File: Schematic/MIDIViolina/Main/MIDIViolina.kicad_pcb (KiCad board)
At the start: 2 copper layers, 148.6 x 100.3 mm, 156 parts, among them J1 Motor, J10 STEPPER OUT, J11 Solenoid, J12 Solenoid, J13 Solenoid, J14 Solenoid, J15 Solenoid, J16 Solenoid, J17 Solenoid, J18 Solenoid, J19 Solenoid, J2 Motor, J20 Solenoid, J21 Solenoid, J22 Solenoid, J23 Solenoid, J24 Solenoid, J25 Solenoid, J26 Solenoid, J27 Solenoid, J28 Solenoid, J29 Solenoid, J3 Motor, J30 Solenoid, J31 Solenoid, J32 Solenoid, J33 Solenoid, J34 Solenoid, J35 Solenoid, J36 Solenoid, J37 Solenoid, J38 Solenoid, J39 Solenoid, J4 Motor, J40 Solenoid, J41 Solenoid, J42 Solenoid, J5 Power in, J6 MSB 2, J7 Solenoid, J8 Microstep Bridge, J9 MIDI I/O, Q1 IRF540N, Q10 IRF540N, Q11 IRF540N, Q12 IRF540N, Q13 IRF540N, Q14 IRF540N, Q15 IRF540N, Q16 IRF540N, Q17 IRF540N, Q18 IRF540N, Q19 IRF540N, Q2 IRF540N, Q20 IRF540N, Q21 IRF540N, Q22 IRF540N, Q23 IRF540N, Q24 IRF540N, Q25 IRF540N, Q26 IRF540N, Q27 IRF540N, Q28 IRF540N, Q29 IRF540N, Q3 IRF540N, Q30 IRF540N, Q31 IRF540N, Q32 IRF540N, Q33 IRF540N, Q34 IRF540N, Q35 IRF540N, Q36 IRF540N, Q37 IRF540N, Q4 IRF540N, Q5 IRF540N, Q6 IRF540N, Q7 IRF540N, Q8 IRF540N, Q9 IRF540N, U1 LM7805_TO220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

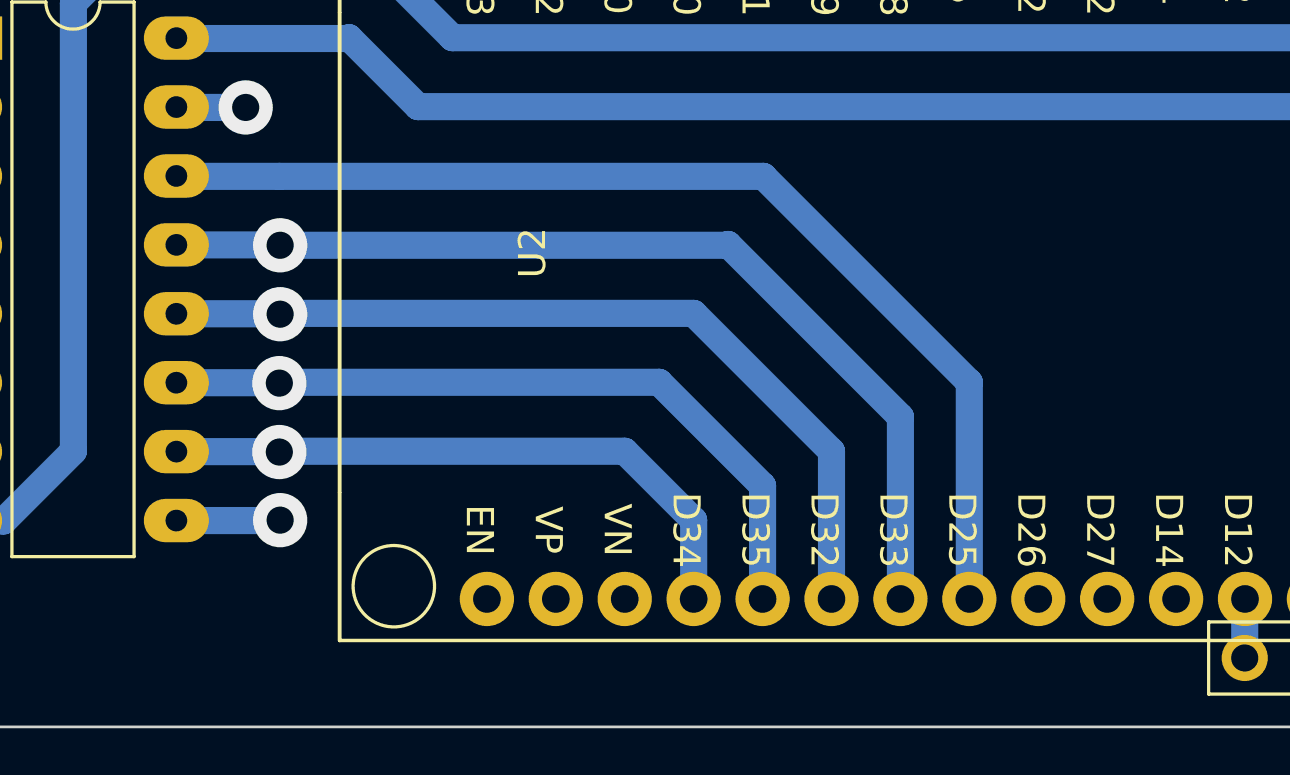
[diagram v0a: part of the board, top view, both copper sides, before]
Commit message: some schematic updates
found a pinout error where I had them hooked up to "input only" pins. Corrected this issue.
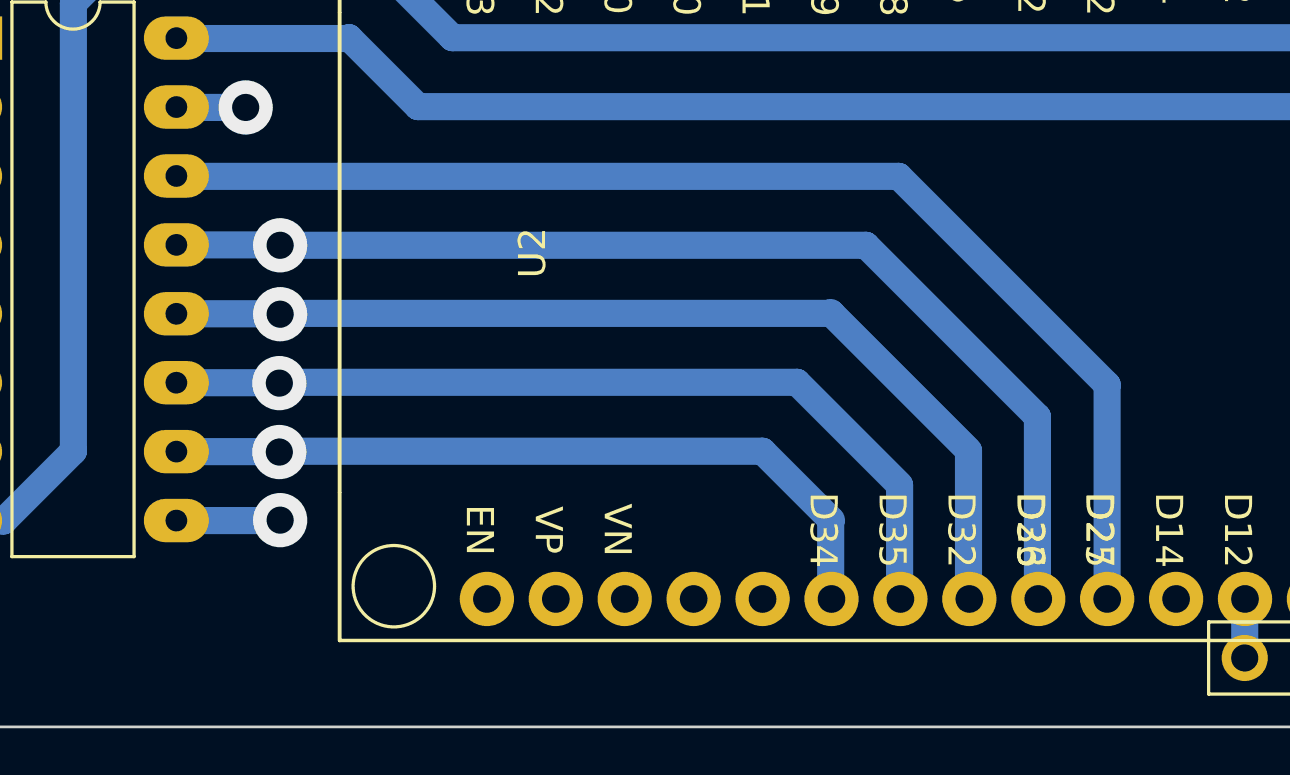
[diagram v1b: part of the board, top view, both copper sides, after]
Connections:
- U2 pad 19: SHIFT CLEAR -> unconnected-(U2-Pad19)
- U2 pad 20: SHIFT CLOCK -> unconnected-(U2-Pad20)
- U2 pad 21: LATCH -> SHIFT CLEAR
- U2 pad 22: OUT ENABLE -> SHIFT CLOCK
- U2 pad 23: SHIFT I/O -> LATCH
- U2 pad 24: unconnected-(U2-Pad24) -> OUT ENABLE
- U2 pad 25: unconnected-(U2-Pad25) -> SHIFT I/O
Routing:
- net SHIFT I/O: track 40.0 -> 45.4 mm
- net LATCH: track 39.0 -> 44.0 mm
- net SHIFT CLEAR: track 30.3 -> 35.4 mm
- net SHIFT CLOCK: track 34.6 -> 39.7 mm
- net OUT ENABLE: track 99.2 -> 104.2 mm
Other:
- board text added: "N:U Input Only"

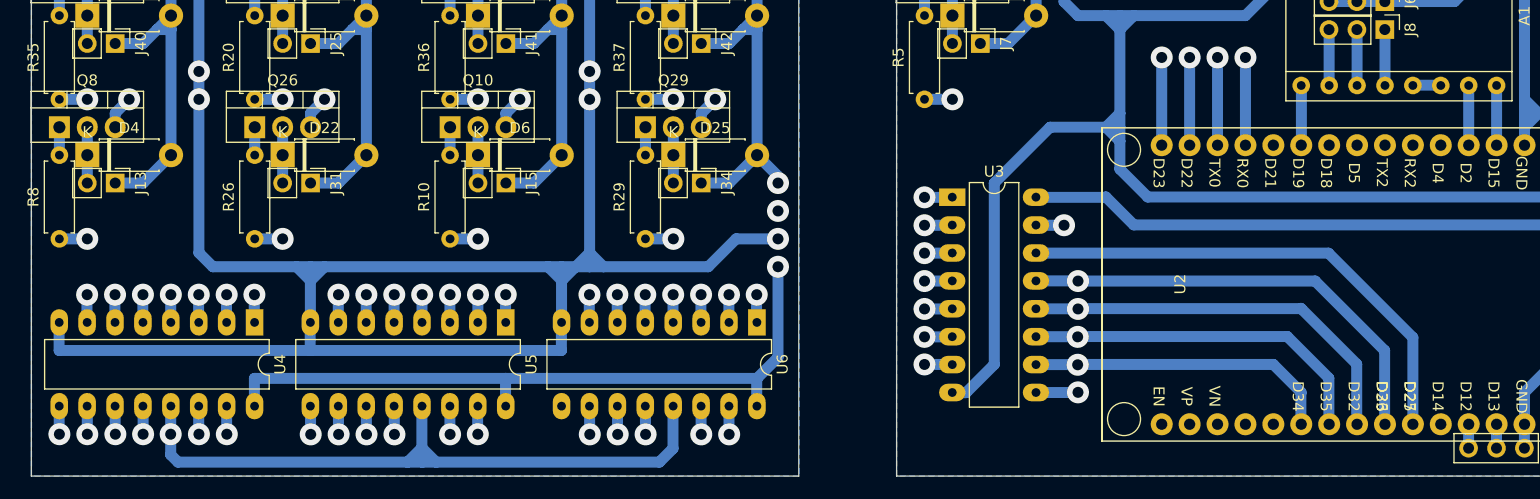
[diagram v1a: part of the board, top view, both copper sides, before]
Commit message: fix pin routing problems
added extra thru-vias and corrected pinouts
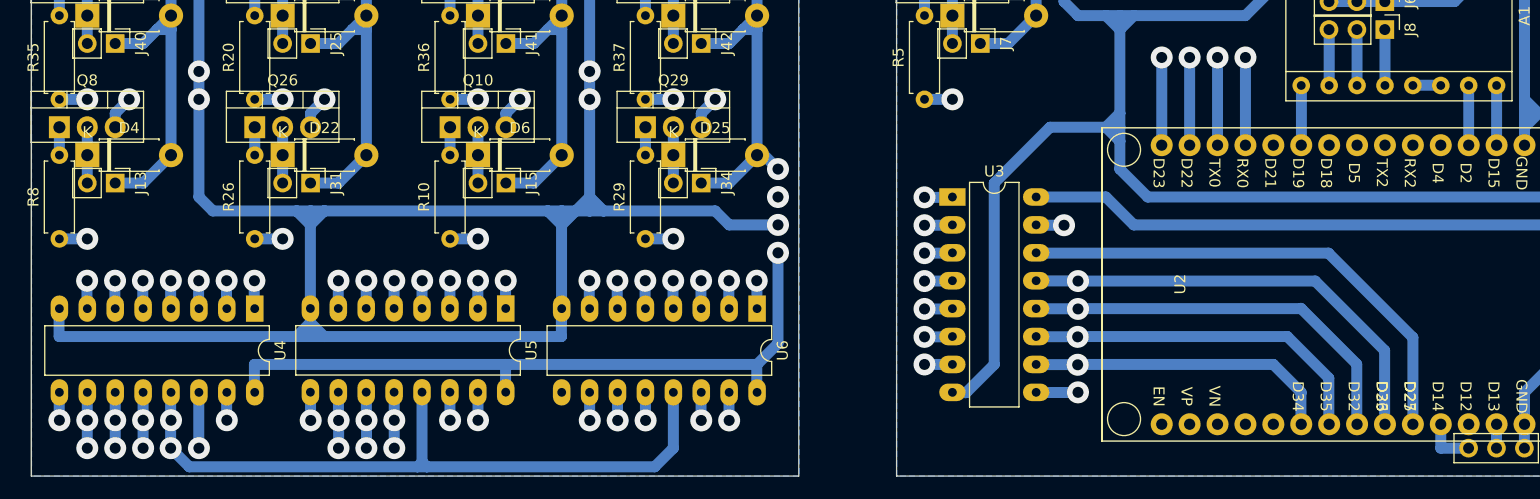
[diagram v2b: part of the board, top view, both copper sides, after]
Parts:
- moved U5 1.27 mm to (113.0, 124.4)
- moved U4 1.26 mm to (90.2, 124.5)
- moved U6 1.26 mm to (135.9, 124.5)
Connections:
- U2 pad 26: unconnected-(U2-Pad26) -> Net-(J9-Pad4)
- U2 pad 27: Net-(J9-Pad4) -> unconnected-(U2-Pad27)
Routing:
- net SHIFT CLOCK: track 39.7 -> 44.8 mm, vias 4 -> 6
- net LATCH: track 44.0 -> 49.1 mm, vias 4 -> 6
- net SHIFT CLEAR: track 35.4 -> 40.4 mm, vias 4 -> 6
- net Net-(U3-Pad9): track 6.37 -> 8.92 mm
- net Net-(J9-Pad4): track 2.54 -> 4.70 mm
- net GND: track 712.0 -> 713.8 mm
- net OUT ENABLE: track 104.2 -> 105.6 mm, vias 2 -> 3
- net +24V: track 800.8 -> 799.9 mm

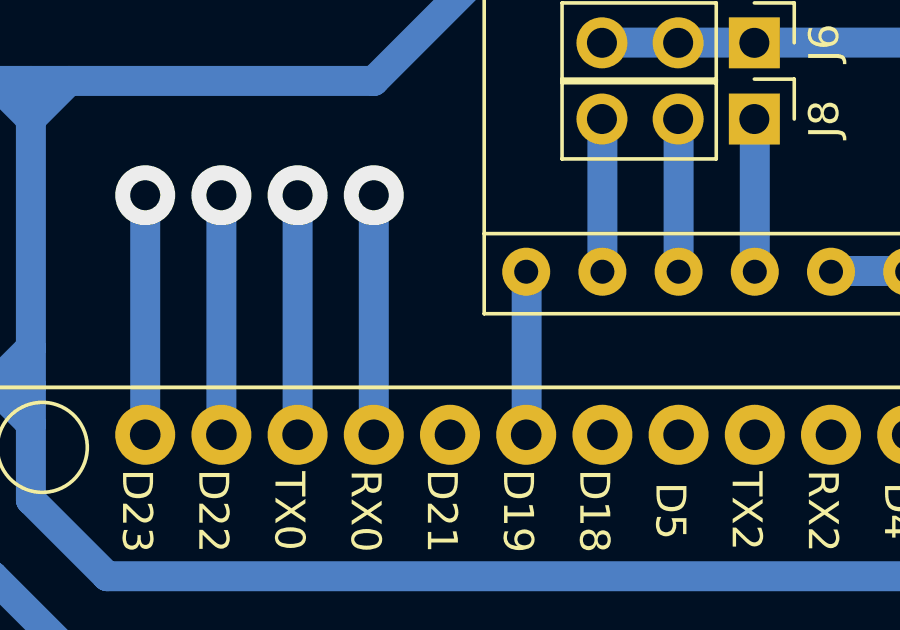
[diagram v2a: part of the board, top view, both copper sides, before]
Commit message: update PCB and added rosen wheel
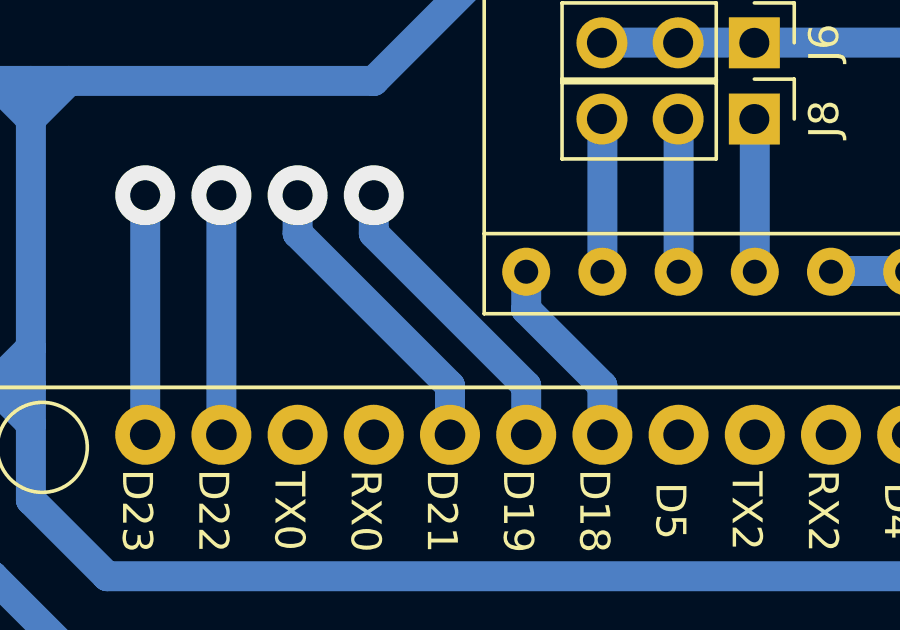
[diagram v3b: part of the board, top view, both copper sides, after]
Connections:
- U2 pad 10: /Enable -> /Motor 4
- U2 pad 11: unconnected-(U2-Pad11) -> /Motor 1
- U2 pad 12: /Motor 4 -> unconnected-(U2-Pad12)
- U2 pad 13: /Motor 1 -> unconnected-(U2-Pad13)
- U2 pad 9: unconnected-(U2-Pad9) -> /Enable
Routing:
- net /Motor 4: track 100.9 -> 103.0 mm
- net /Motor 1: track 78.2 -> 80.3 mm
- net /Enable: track 5.45 -> 6.49 mm
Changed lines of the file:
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@@
   (net 140 "Net-(J9-Pad3)")
   (net 141 "unconnected-(U2-Pad8)")
-  (net 142 "unconnected-(U2-Pad9)")
-  (net 143 "unconnected-(U2-Pad11)")
+  (net 142 "unconnected-(U2-Pad12)")
+  (net 143 "unconnected-(U2-Pad13)")
   (net 144 "Net-(J9-Pad4)")
   (net 145 "Net-(Q37-Pad1)")
@@
       (net 141 "unconnected-(U2-Pad8)") (pinfunction "D5") (pintype "bidirectional+no_connect"))
     (pad "9" thru_hole circle (at -12.335 3.81 270) (size 2 2) (drill 1.02) (layers *.Cu *.Mask)
-      (net 142 "unconnected-(U2-Pad9)") (pinfunction "D18") (pintype "bidirectional+no_connect"))
+      (net 132 "/Enable") (pinfunction "D18") (pintype "bidirectional"))
     (pad "10" thru_hole circle (at -12.335 6.35 270) (size 2 2) (drill 1.02) (layers *.Cu *.Mask)
-      (net 132 "/Enable") (pinfunction "D19") (pintype "bidirectional"))
+      (net 7 "/Motor 4") (pinfunction "D19") (pintype "bidirectional"))
     (pad "11" thru_hole circle (at -12.335 8.89 270) (size 2 2) (drill 1.02) (layers *.Cu *.Mask)
-      (net 143 "unconnected-(U2-Pad11)") (pinfunction "D21") (pintype "bidirectional+no_connect"))
+      (net 5 "/Motor 1") (pinfunction "D21") (pintype "bidirectional"))
     (pad "12" thru_hole circle (at -12.335 11.43 270) (size 2 2) (drill 1.02) (layers *.Cu *.Mask)
-      (net 7 "/Motor 4") (pinfunction "RX0") (pintype "input"))
+      (net 142 "unconnected-(U2-Pad12)") (pinfunction "RX0") (pintype "input+no_connect"))
     (pad "13" thru_hole circle (at -12.335 13.97 270) (size 2 2) (drill 1.02) (layers *.Cu *.Mask)
-      (net 5 "/Motor 1") (pinfunction "TX0") (pintype "output"))
+      (net 143 "unconnected-(U2-Pad13)") (pinfunction "TX0") (pintype "output+no_connect"))
     (pad "14" thru_hole circle (at -12.335 16.51 270) (size 2 2) (drill 1.02) (layers *.Cu *.Mask)
       (net 6 "/Motor 3") (pinfunction "D22") (pintype "bidirectional"))
@@
   (segment (start 212.09 44.45) (end 204.47 44.45) (width 1) (layer "B.Cu") (net 5))
   (segment (start 204.47 44.45) (end 203.2 45.72) (width 1) (layer "B.Cu") (net 5))
-  (segment (start 177.8 109.585) (end 177.8 101.6) (width 1) (layer "B.Cu") (net 5))
   (segment (start 196.85 78.74) (end 201.93 73.66) (width 1) (layer "B.Cu") (net 5))
   (segment (start 212.09 73.66) (end 213.36 72.39) (width 1) (layer "B.Cu") (net 5))
@@
   (segment (start 203.2 45.72) (end 203.2 46.99) (width 1) (layer "B.Cu") (net 5))
   (segment (start 213.36 72.39) (end 213.36 45.72) (width 1) (layer "B.Cu") (net 5))
+  (segment (start 177.8 102.87) (end 177.8 101.6) (width 1) (layer "B.Cu") (net 5))
   (segment (start 203.2 49.53) (end 203.2 46.99) (width 1) (layer "B.Cu") (net 5))
   (segment (start 201.93 73.66) (end 212.09 73.66) (width 1) (layer "B.Cu") (net 5))
+  (segment (start 182.88 107.95) (end 177.8 102.87) (width 1) (layer "B.Cu") (net 5))
   (segment (start 190.5 78.74) (end 196.85 78.74) (width 1) (layer "B.Cu") (net 5))
+  (segment (start 182.88 109.585) (end 182.88 107.95) (width 1) (layer "B.Cu") (net 5))
   (segment (start 189.23 81.28) (end 189.23 80.01) (width 1) (layer "B.Cu") (net 5))
   (via (at 186.69 81.28) (size 2) (drill 1) (layers "F.Cu" "B.Cu") (net 6))
@@
   (segment (start 213.36 41.91) (end 215.9 44.45) (width 1) (layer "B.Cu") (net 7))
   (segment (start 213.36 76.2) (end 203.2 76.2) (width 1) (layer "B.Cu") (net 7))
+  (segment (start 185.42 109.585) (end 185.42 107.95) (width 1) (layer "B.Cu") (net 7))
   (segment (start 189.23 41.91) (end 213.36 41.91) (width 1) (layer "B.Cu") (net 7))
   (segment (start 203.2 76.2) (end 198.12 81.28) (width 1) (layer "B.Cu") (net 7))
   (segment (start 186.69 44.45) (end 189.23 41.91) (width 1) (layer "B.Cu") (net 7))
   (segment (start 198.12 81.28) (end 191.77 81.28) (width 1) (layer "B.Cu") (net 7))
+  (segment (start 185.42 107.95) (end 180.34 102.87) (width 1) (layer "B.Cu") (net 7))
+  (segment (start 185.435 109.57) (end 185.42 109.585) (width 1) (layer "B.Cu") (net 7))
+  (segment (start 180.34 102.87) (end 180.34 101.6) (width 1) (layer "B.Cu") (net 7))
   (segment (start 215.9 73.66) (end 213.36 76.2) (width 1) (layer "B.Cu") (net 7))
-  (segment (start 180.34 109.585) (end 180.34 101.6) (width 1) (layer "B.Cu") (net 7))
   (segment (start 215.9 44.45) (end 215.9 73.66) (width 1) (layer "B.Cu") (net 7))
   (via (at 153.67 54.61) (size 2) (drill 1) (layers "F.Cu" "B.Cu") (net 8))
@@
   (segment (start 190.515 90.18) (end 190.505 90.17) (width 1) (layer "B.Cu") (net 131))
   (segment (start 190.5 91.44) (end 190.5 88.9) (width 1) (layer "B.Cu") (net 131))
-  (segment (start 185.435 109.57) (end 185.42 109.585) (width 1) (layer "B.Cu") (net 132))
-  (segment (start 185.435 104.14) (end 185.435 109.57) (width 1) (layer "B.Cu") (net 132))
+  (segment (start 187.96 109.585) (end 187.96 107.95) (width 1) (layer "B.Cu") (net 132))
+  (segment (start 187.96 107.95) (end 185.42 105.41) (width 1) (layer "B.Cu") (net 132))
+  (segment (start 185.42 105.41) (end 185.42 104.15) (width 1) (layer "B.Cu") (net 132))
   (segment (start 187.96 104.135) (end 187.96 99.06) (width 1) (layer "B.Cu") (net 133))
   (segment (start 187.96 99.06) (end 187.945 99.045) (width 1) (layer "B.Cu") (net 133))
